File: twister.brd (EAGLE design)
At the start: 101.6 x 81.3 mm, 30 parts, among them IC1 A3967SLB, U1 ARDUINO_SHIELDNOHOLES

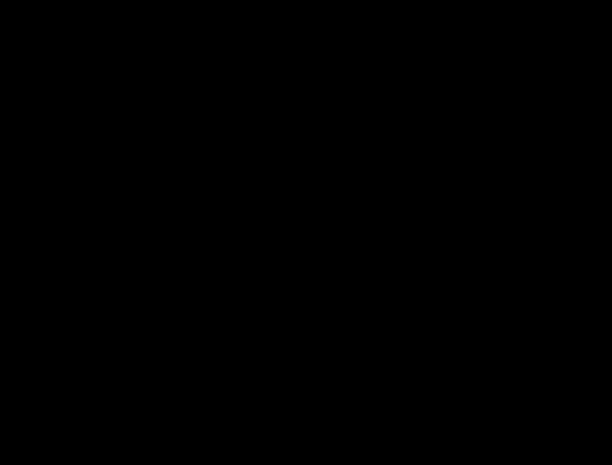
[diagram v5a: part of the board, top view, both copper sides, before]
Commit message: Put together first PCB, started documenting improvements.
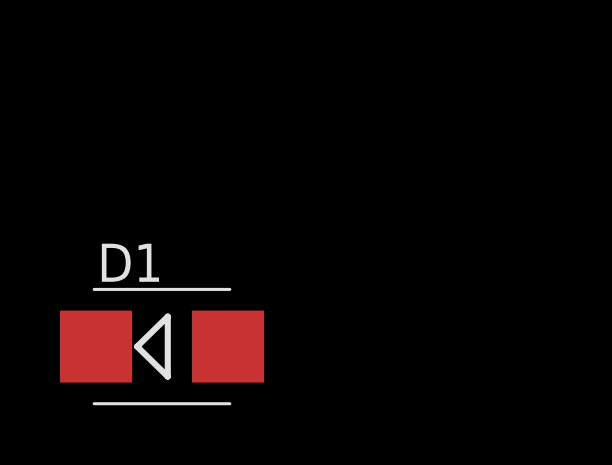
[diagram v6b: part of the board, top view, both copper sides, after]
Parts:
- added D1: DIODE_SMB, twister_clean:SMB
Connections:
- new net A: D1.C, LCD_MODULE.15
- net +5V: now also D1.A; no longer LCD_MODULE.15
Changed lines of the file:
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@@
 <?xml version="1.0" encoding="utf-8"?>
 <!DOCTYPE eagle SYSTEM "eagle.dtd">
-<eagle version="6.5.0">
+<eagle version="6.4">
 <drawing>
 <settings>
@@
 <layer number="15" name="Route15" color="4" fill="6" visible="no" active="no"/>
 <layer number="16" name="Bottom" color="9" fill="1" visible="yes" active="yes"/>
-<layer number="17" name="Pads" color="10" fill="1" visible="yes" active="yes"/>
-<layer number="18" name="Vias" color="10" fill="1" visible="yes" active="yes"/>
-<layer number="19" name="Unrouted" color="6" fill="1" visible="yes" active="yes"/>
-<layer number="20" name="Dimension" color="15" fill="1" visible="yes" active="yes"/>
-<layer number="21" name="tPlace" color="27" fill="1" visible="yes" active="yes"/>
-<layer number="22" name="bPlace" color="14" fill="1" visible="yes" active="yes"/>
-<layer number="23" name="tOrigins" color="15" fill="1" visible="yes" active="yes"/>
-<layer number="24" name="bOrigins" color="15" fill="1" visible="yes" active="yes"/>
-<layer number="25" name="tNames" color="7" fill="1" visible="yes" active="yes"/>
-<layer number="26" name="bNames" color="7" fill="1" visible="yes" active="yes"/>
-<layer number="27" name="tValues" color="7" fill="1" visible="yes" active="yes"/>
-<layer number="28" name="bValues" color="7" fill="1" visible="yes" active="yes"/>
+<layer number="17" name="Pads" color="10" fill="1" visible="no" active="yes"/>
+<layer number="18" name="Vias" color="10" fill="1" visible="no" active="yes"/>
+<layer number="19" name="Unrouted" color="6" fill="1" visible="no" active="yes"/>
+<layer number="20" name="Dimension" color="15" fill="1" visible="no" active="yes"/>
+<layer number="21" name="tPlace" color="27" fill="1" visible="no" active="yes"/>
+<layer number="22" name="bPlace" color="14" fill="1" visible="no" active="yes"/>
+<layer number="23" name="tOrigins" color="15" fill="1" visible="no" active="yes"/>
+<layer number="24" name="bOrigins" color="15" fill="1" visible="no" active="yes"/>
+<layer number="25" name="tNames" color="7" fill="1" visible="no" active="yes"/>
+<layer number="26" name="bNames" color="7" fill="1" visible="no" active="yes"/>
+<layer number="27" name="tValues" color="7" fill="1" visible="no" active="yes"/>
+<layer number="28" name="bValues" color="7" fill="1" visible="no" active="yes"/>
 <layer number="29" name="tStop" color="7" fill="3" visible="no" active="yes"/>
 <layer number="30" name="bStop" color="7" fill="6" visible="no" active="yes"/>
@@
 <attribute name="VALUE" x="25.0825" y="0.3175" size="1.27" layer="27" font="vector" ratio="18"/>
 </element>
+<element name="D1" library="twister_clean" package="SMB" value="DIODE_SMB" x="-1.27" y="-24.13"/>
 </elements>
 <signals>
@@
 <contactref element="LCD_MODULE" pad="1"/>
 <contactref element="LCD_MODULE" pad="5"/>
-<polygon width="0.254" layer="16">
+<polygon width="0.254" layer="16" isolate="0.254" thermals="no">
 <vertex x="0" y="77.216"/>
 <vertex x="0" y="51.816"/>
@@
 <contactref element="R4" pad="1"/>
 <contactref element="R1" pad="LEFT"/>
-<contactref element="LCD_MODULE" pad="15"/>
 <wire x1="84.074" y1="29.21" x2="83.160390625" y2="29.21" width="0.4064" layer="1"/>
 <contactref element="CONTRAST" pad="1"/>
@@
 <contactref element="R2" pad="LEFT"/>
 <contactref element="U1" pad="5V"/>
-<polygon width="0.254" layer="1">
+<polygon width="0.254" layer="1" isolate="0.254" thermals="no">
 <vertex x="0" y="77.216"/>
 <vertex x="0" y="51.816"/>
@@
 </polygon>
 <contactref element="LCD_MODULE" pad="2"/>
+<contactref element="D1" pad="A"/>
+<wire x1="18.1864" y1="2.54" x2="0.93" y2="-24.13" width="0" layer="19" extent="1-1"/>
 </signal>
 <signal name="N$1">
@@
 <wire x1="31.27" y1="8.255" x2="33.4264" y2="8.255" width="0.4064" layer="1"/>
 </signal>
+<signal name="A">
+<contactref element="D1" pad="C"/>
+<contactref element="LCD_MODULE" pad="15"/>
+<wire x1="-3.47" y1="-24.13" x2="42.158" y2="44.2" width="0" layer="19" extent="1-1"/>
+</signal>
 </signals>
